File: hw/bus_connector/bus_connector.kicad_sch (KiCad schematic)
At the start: 11 parts, among them J1 DB9_Top, J2 DB9_Left, J3 DB9_Right

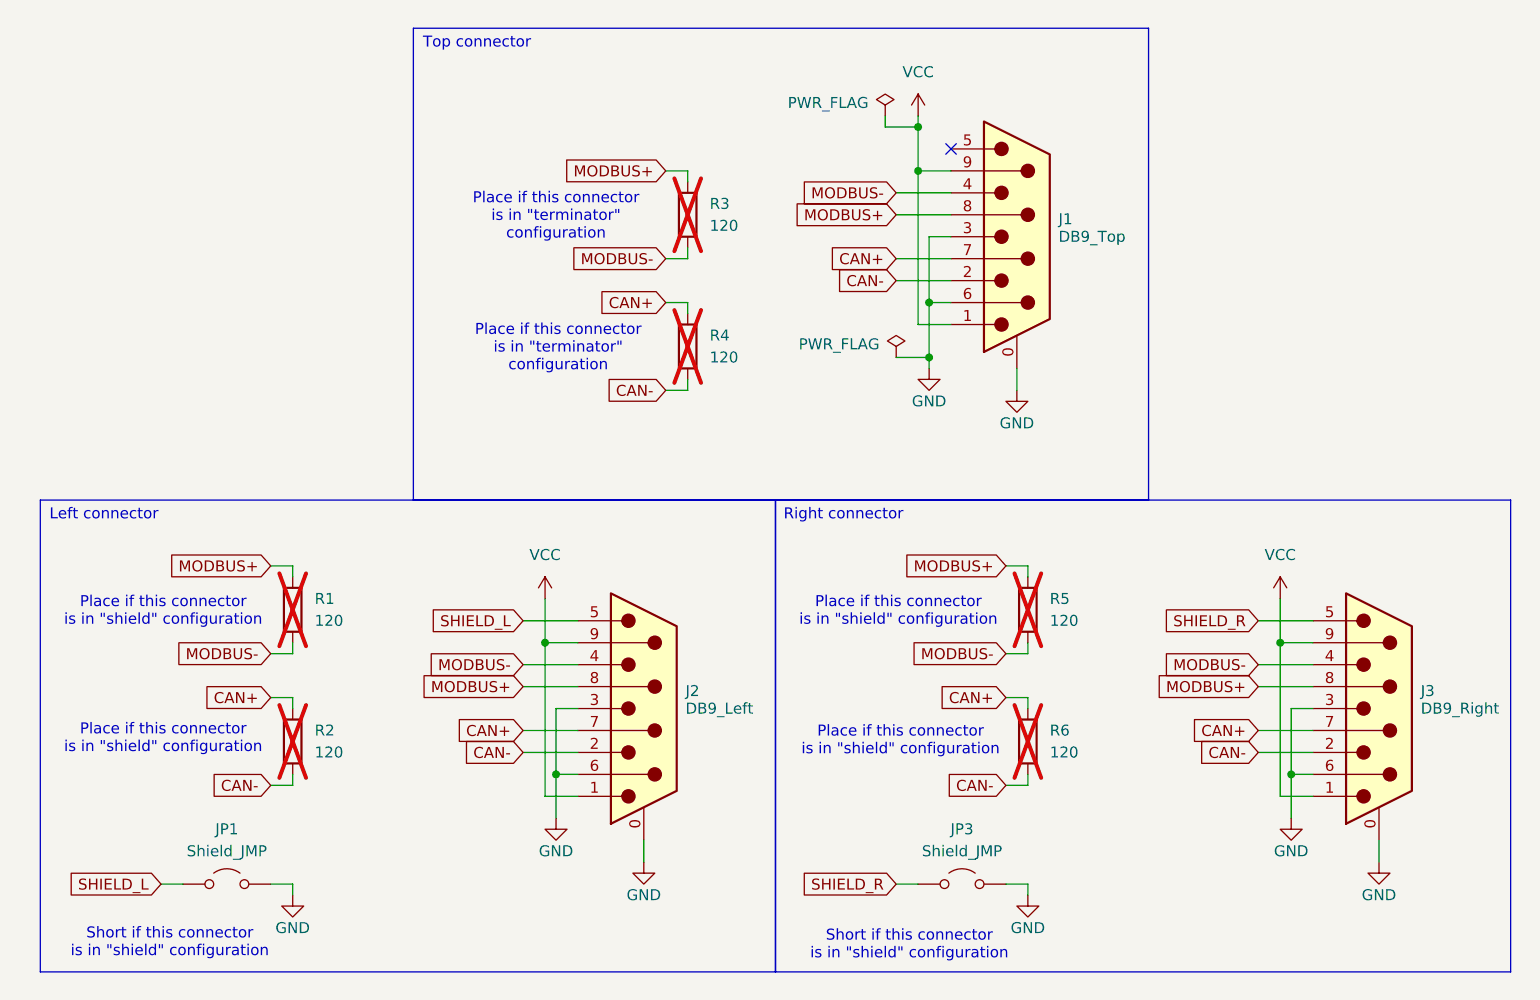
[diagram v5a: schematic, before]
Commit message: Simplify bus connector
Signed-off-by: Mateusz Pająk <22417805+Tai-Min@users.noreply.github.com>
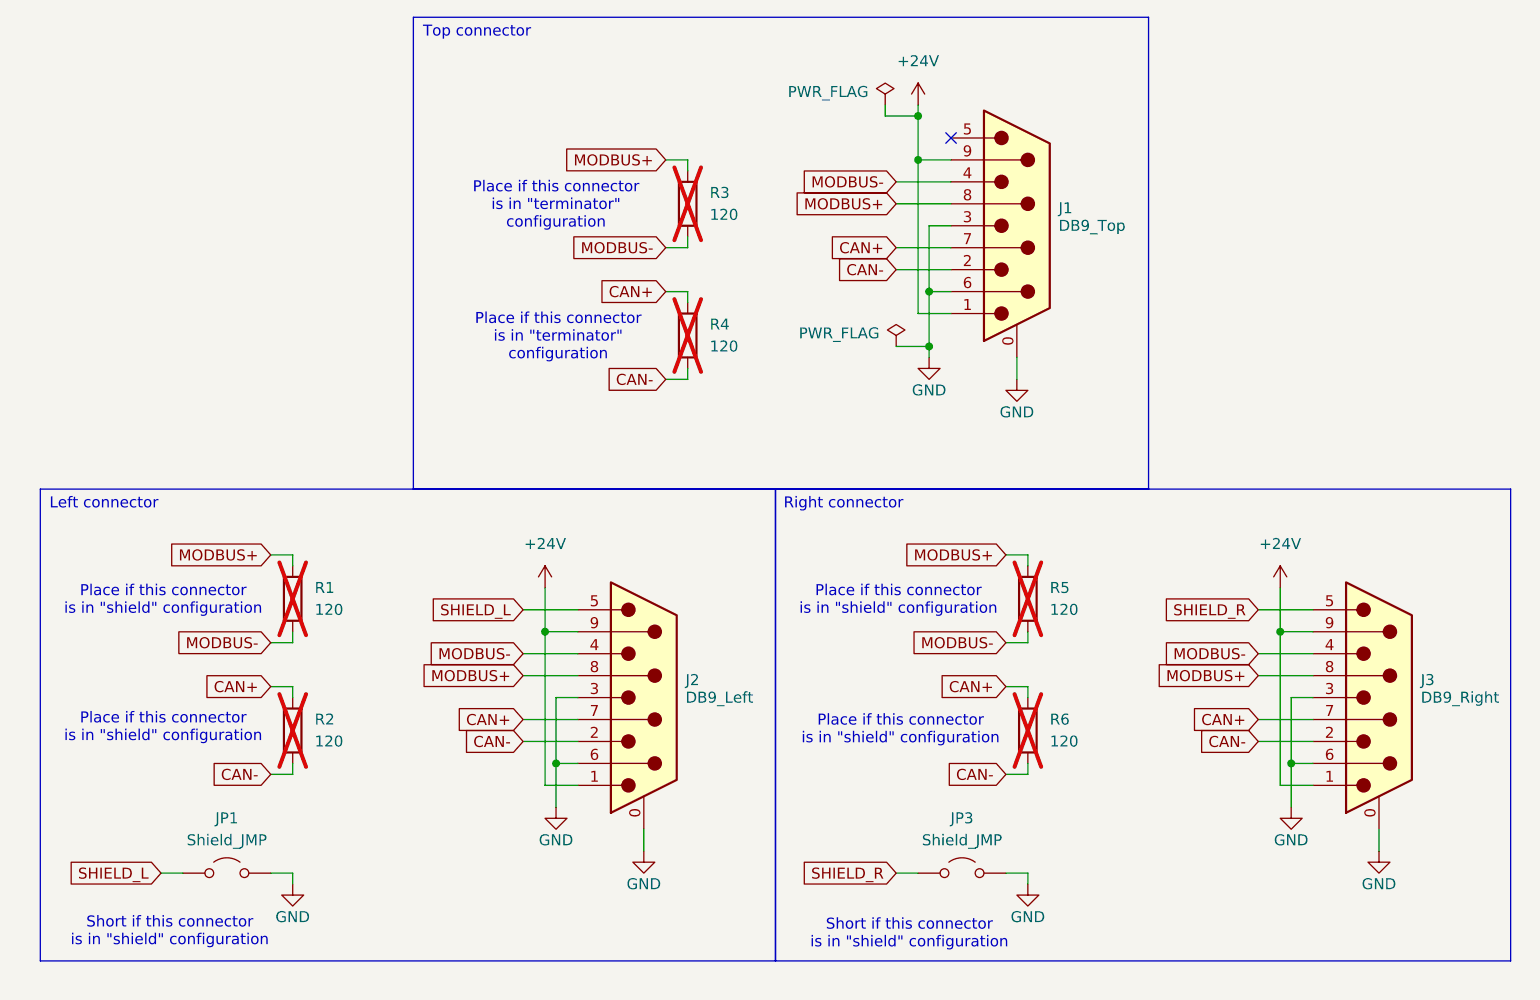
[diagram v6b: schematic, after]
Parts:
- R1, R2, R3, R4, R5, R6: footprint Resistor_SMD:R_1206_3216Metric_Pad1.30x1.75mm_HandSolder -> KMur_kicad_lib:RLC_1206_3216Metric
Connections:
- net VCC renamed +24V
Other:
- moved on the sheet: J1, J2, J3, JP1, JP3, R1, R2, R3, R4, R5, R6
